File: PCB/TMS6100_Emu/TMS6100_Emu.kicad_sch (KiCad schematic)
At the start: 17 parts, among them J1 Conn_02x14_Counter_Clockwise, Q1 BSS138, U1 XC6206P322MR, U2 STM32G051F8P6

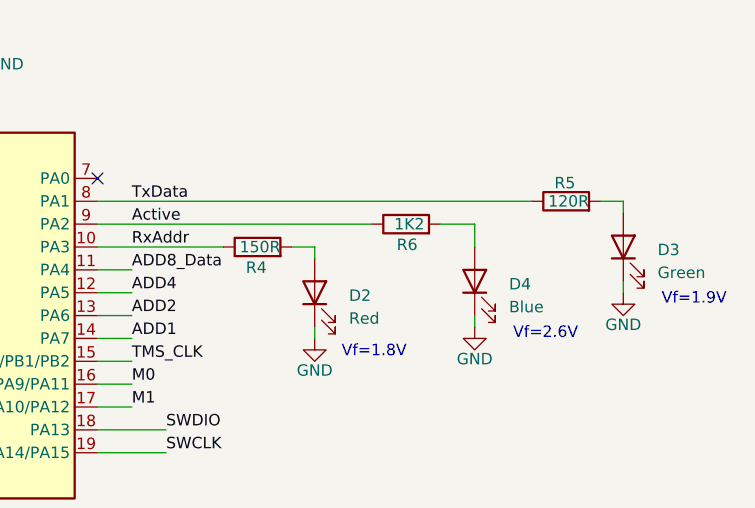
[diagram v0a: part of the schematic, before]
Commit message: Minor fix to Basic program, adjust blue LED resistor value
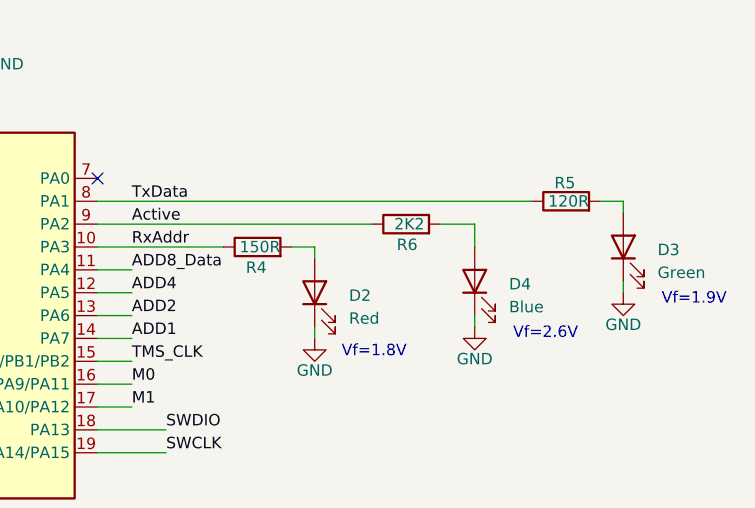
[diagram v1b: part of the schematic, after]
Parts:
- R6: value 1K2 -> 2K2
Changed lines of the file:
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@@
 			)
 		)
-		(property "Value" "1K2"
+		(property "Value" "2K2"
 			(at 183.642 49.53 90)
 			(effects
